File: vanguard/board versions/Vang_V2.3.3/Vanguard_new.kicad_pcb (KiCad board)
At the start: 4 copper layers, 57.6 x 40 mm, 94 parts, among them J1 USB_C_Receptacle_USB2.0_16P, J2 Micro_SD_Card_Det1, J3 Conn_02x03_Odd_Even, J4 Conn_01x03, J5 Conn_01x03, J6 Conn_01x03, J7 Conn_01x02_Pin, Q4 BSS138, U1 TPS82130, U10 ATmega4809-A, U12 AP2112K-3.3, U3 ATSAMD11D14A-M, U4 BMP390L, U5 BD1020HFV-TR, U6 AT25DF641A-SH-T, U8 BNO055, U9 TPS61092, Y1 Crystal

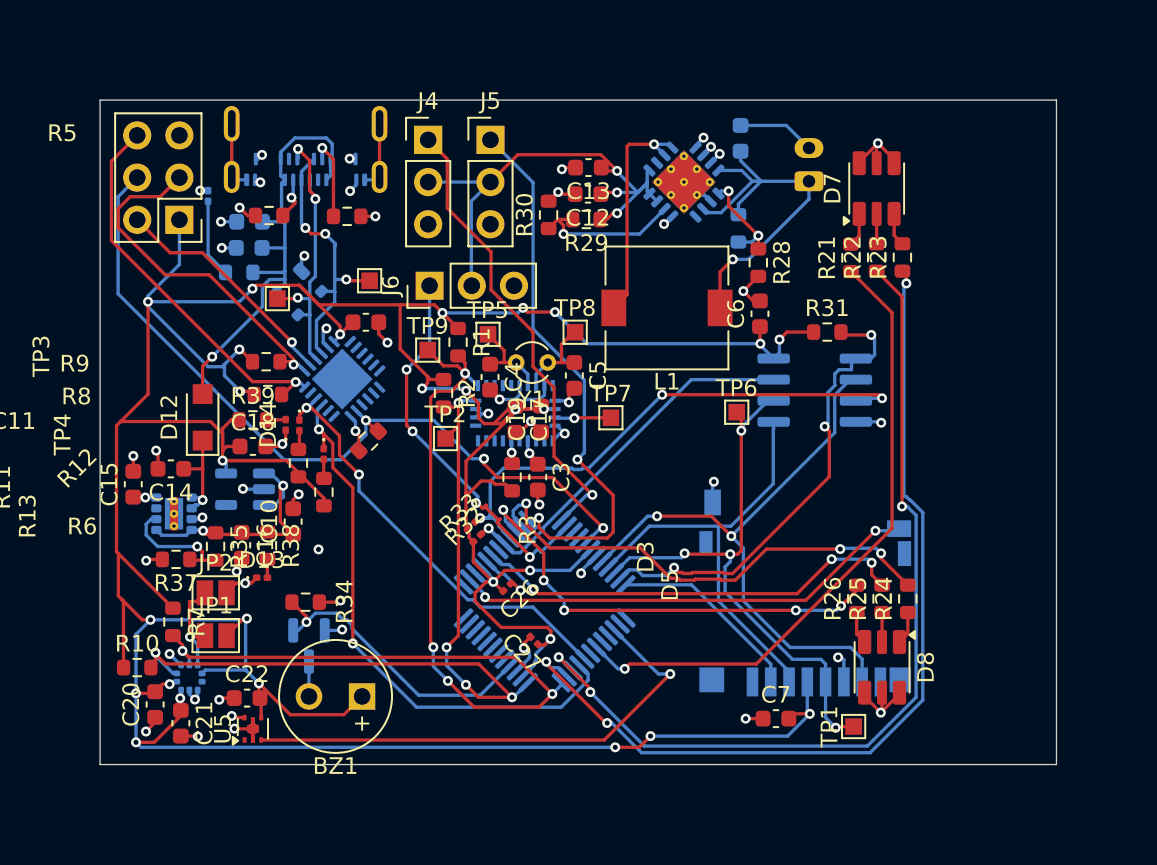
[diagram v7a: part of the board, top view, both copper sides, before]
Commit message: added power switch
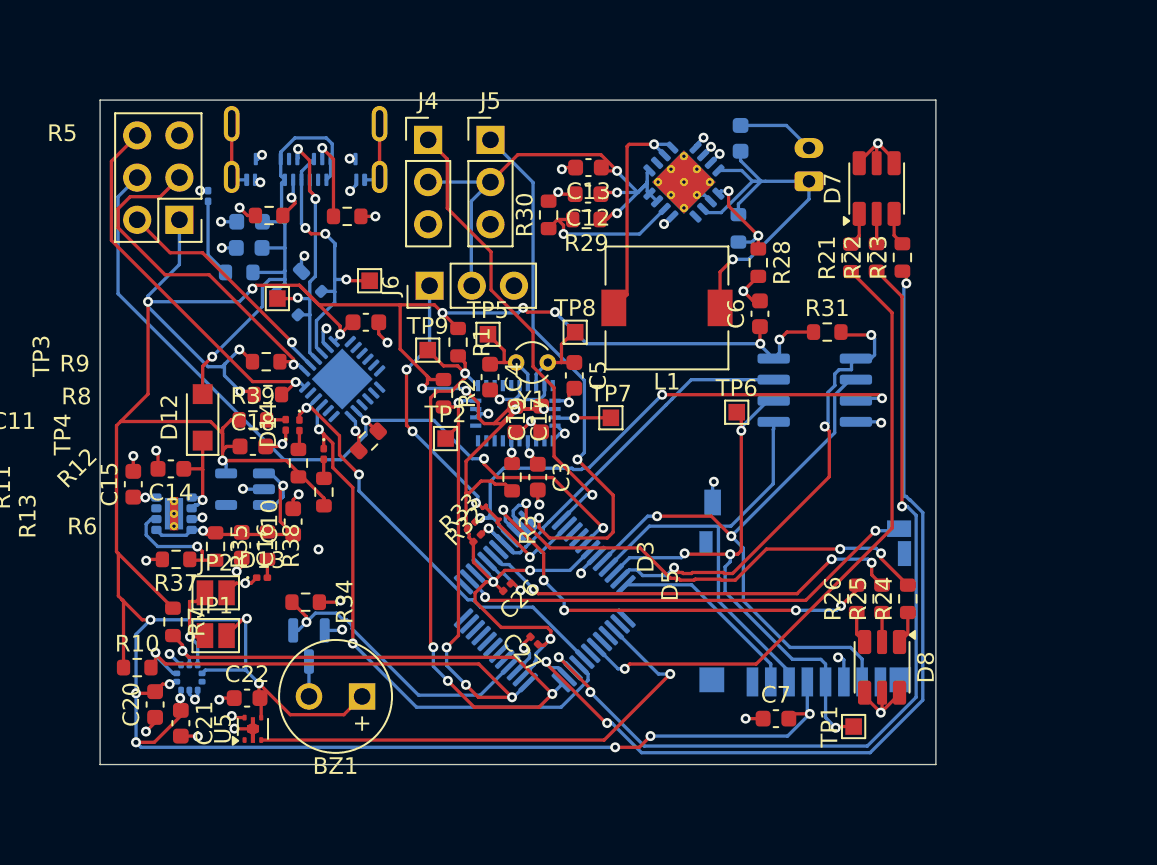
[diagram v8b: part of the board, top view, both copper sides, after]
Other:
- board size 57.6 x 40 mm -> 50.3 x 40 mm
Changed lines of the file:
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@@
 	(gr_rect
 		(start 145.712652 99.837652)
-		(end 203.287652 139.837652)
+		(end 196.027652 139.837652)
 		(stroke
 			(width 0.05)
